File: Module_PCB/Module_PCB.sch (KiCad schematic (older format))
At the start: 102 parts, among them J1 ISP, J2 US, J3 DS, Q1 HSS2307, Q2 BSS123, U1 W25Q16JV, U2 AP1117-33, U3 TPS563200, U5 ATmega328P-AU, U7 74LVC1G34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

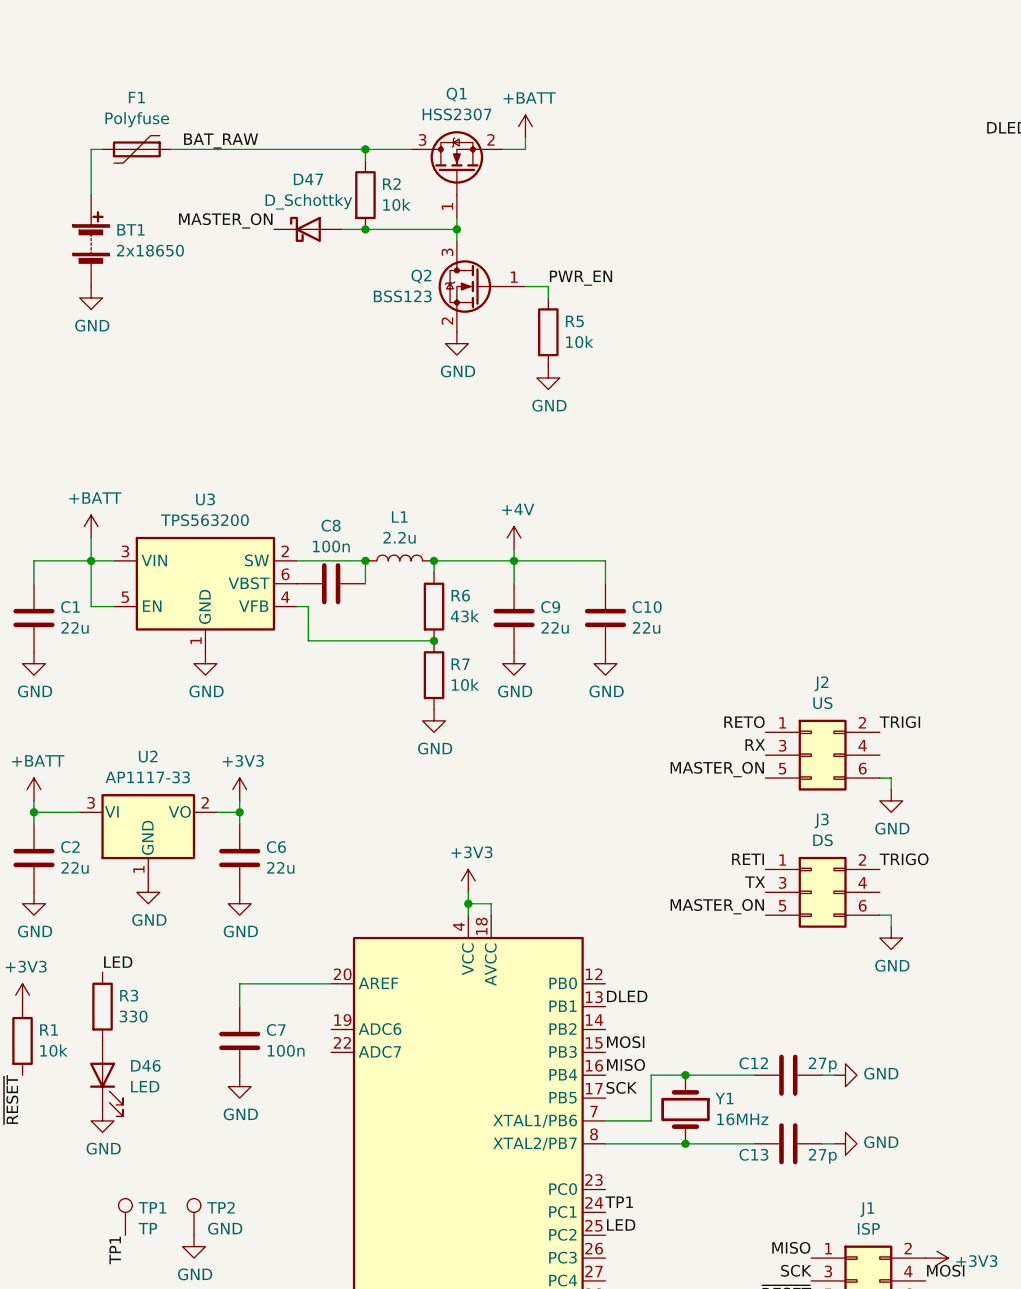
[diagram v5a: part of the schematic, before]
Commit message: Added voltage divider to measure the battery voltage
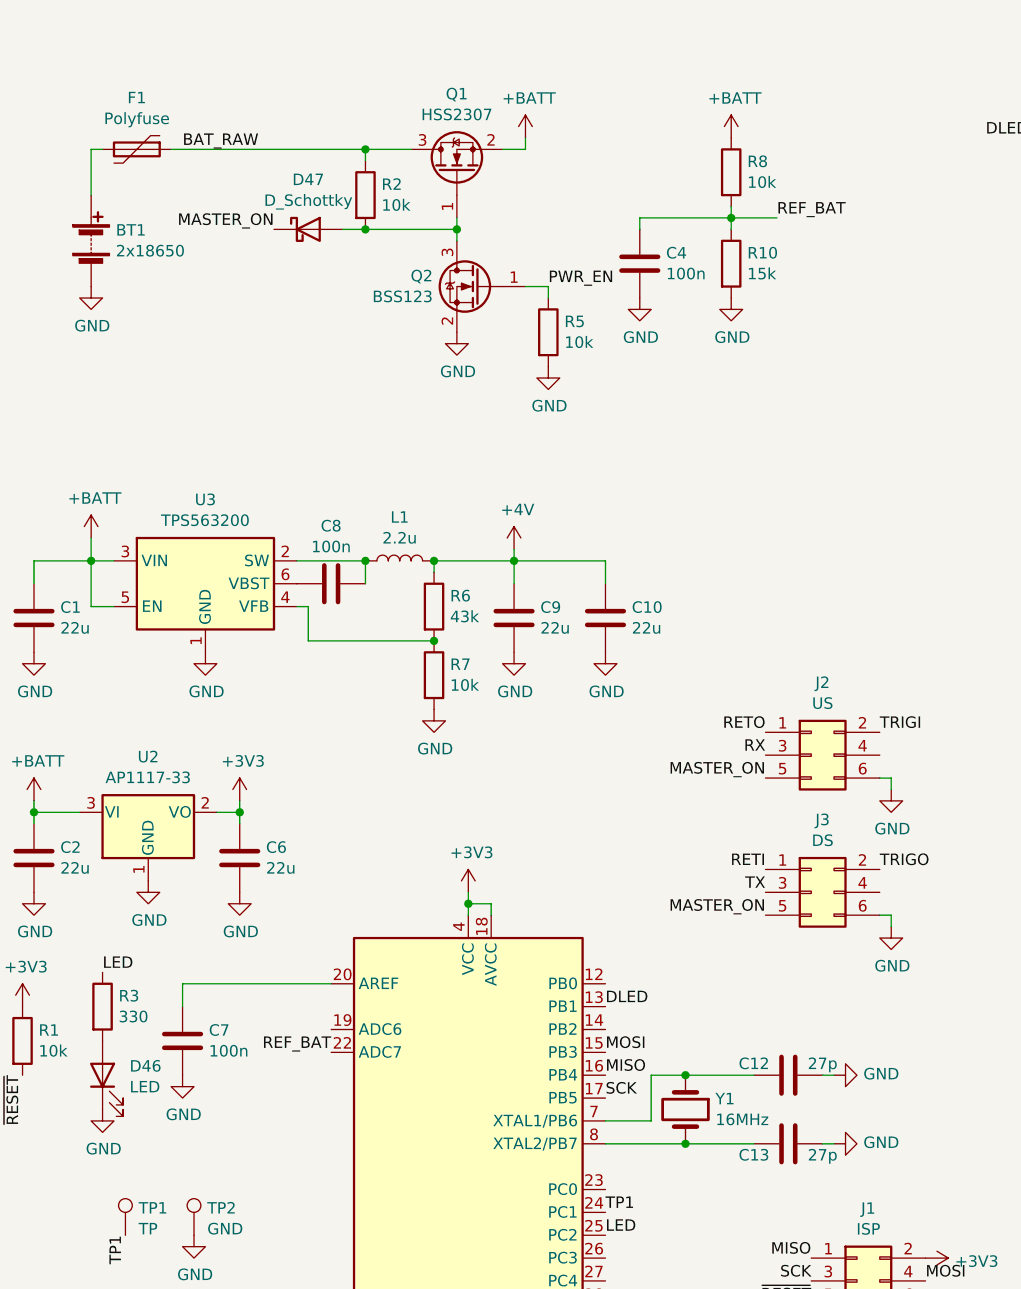
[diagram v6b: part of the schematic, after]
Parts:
- added C4: 100n, Capacitor_SMD:C_0603_1608Metric, symbol Device:C
- added R10: 15k, Resistor_SMD:R_0603_1608Metric, symbol Device:R
- added R8: 10k, Resistor_SMD:R_0603_1608Metric, symbol Device:R
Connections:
- net +BATT: now also R8.1
- net GND: now also C4.2, R10.2
- net REF_BAT: now reaches U5.22 (ADC7)
- net REF_BAT: now also C4.1, R10.1, R8.2
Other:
- moved on the sheet: C7
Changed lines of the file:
@@
 Wire Wire Line
 	2600 4350 2600 4400
-$Comp
-L Device:C C7
-U 1 1 60D68DB6
-P 1600 4950
-F 0 "C7" H 1715 4996 50  0000 L CNN
-F 1 "100n" H 1715 4905 50  0000 L CNN
-F 2 "Capacitor_SMD:C_0603_1608Metric" H 1638 4800 50  0001 C CNN
-F 3 "~" H 1600 4950 50  0001 C CNN
-F 4 "CC0603KRX7R0BB104" H 1600 4950 50  0001 C CNN "MPN"
-F 5 "YAGEO" H 1600 4950 50  0001 C CNN "Manufacturer"
-	1    1600 4950
-	1    0    0    -1
-$EndComp
-Wire Wire Line
-	2000 4700 1600 4700
-Wire Wire Line
-	1600 4700 1600 4800
-$Comp
-L power:GND #PWR018
-U 1 1 60D69990
-P 1600 5100
-F 0 "#PWR018" H 1600 4850 50  0001 C CNN
-F 1 "GND" H 1605 4927 50  0000 C CNN
-F 2 "" H 1600 5100 50  0001 C CNN
-F 3 "" H 1600 5100 50  0001 C CNN
-	1    1600 5100
-	1    0    0    -1
-$EndComp
 Text Label 3200 5200 0    50   ~ 0
 SCK
@@
 Text Label 5900 7300 0    50   ~ 0
 ~RET_EN
-Text Label 3450 7100 0    50   ~ 0
-~RET_EN
 $Comp
 L power:GND #PWR043
@@
 Wire Wire Line
 	1300 1050 2150 1050
+Text Label 2000 5000 2    50   ~ 0
+REF_BAT
+$Comp
+L power:GND #PWR018
+U 1 1 60D69990
+P 1350 5100
+F 0 "#PWR018" H 1350 4850 50  0001 C CNN
+F 1 "GND" H 1355 4927 50  0000 C CNN
+F 2 "" H 1350 5100 50  0001 C CNN
+F 3 "" H 1350 5100 50  0001 C CNN
+	1    1350 5100
+	1    0    0    -1
+$EndComp
+Wire Wire Line
+	1350 4700 1350 4800
+Wire Wire Line
+	2000 4700 1350 4700
+$Comp
+L Device:C C7
+U 1 1 60D68DB6
+P 1350 4950
+F 0 "C7" H 1465 4996 50  0000 L CNN
+F 1 "100n" H 1465 4905 50  0000 L CNN
+F 2 "Capacitor_SMD:C_0603_1608Metric" H 1388 4800 50  0001 C CNN
+F 3 "~" H 1350 4950 50  0001 C CNN
+F 4 "CC0603KRX7R0BB104" H 1350 4950 50  0001 C CNN "MPN"
+F 5 "YAGEO" H 1350 4950 50  0001 C CNN "Manufacturer"
+	1    1350 4950
+	1    0    0    -1
+$EndComp
+Text Label 3450 7100 0    50   ~ 0
+~RET_EN
+$Comp
+L power:GND #PWR0139
+U 1 1 60E13F4A
+P 3350 1700
+F 0 "#PWR0139" H 3350 1450 50  0001 C CNN
+F 1 "GND" H 3355 1527 50  0000 C CNN
+F 2 "" H 3350 1700 50  0001 C CNN
+F 3 "" H 3350 1700 50  0001 C CNN
+	1    3350 1700
+	1    0    0    -1
+$EndComp
+$Comp
+L Device:C C4
+U 1 1 60E134A1
+P 3350 1550
+F 0 "C4" H 3465 1596 50  0000 L CNN
+F 1 "100n" H 3465 1505 50  0000 L CNN
+F 2 "Capacitor_SMD:C_0603_1608Metric" H 3388 1400 50  0001 C CNN
+F 3 "~" H 3350 1550 50  0001 C CNN
+F 4 "CC0603KRX7R0BB104" H 3350 1550 50  0001 C CNN "MPN"
+F 5 "YAGEO" H 3350 1550 50  0001 C CNN "Manufacturer"
+	1    3350 1550
+	1    0    0    -1
+$EndComp
+Text Label 3950 1350 0    50   ~ 0
+REF_BAT
+Wire Wire Line
+	3750 1350 3950 1350
+Wire Wire Line
+	3750 1350 3750 1400
+Connection ~ 3750 1350
+Wire Wire Line
+	3750 1300 3750 1350
+$Comp
+L power:+BATT #PWR02
+U 1 1 60E007AC
+P 3750 1000
+F 0 "#PWR02" H 3750 850 50  0001 C CNN
+F 1 "+BATT" H 3765 1173 50  0000 C CNN
+F 2 "" H 3750 1000 50  0001 C CNN
+F 3 "" H 3750 1000 50  0001 C CNN
+	1    3750 1000
+	1    0    0    -1
+$EndComp
+$Comp
+L power:GND #PWR030
+U 1 1 60DFEFDA
+P 3750 1700
+F 0 "#PWR030" H 3750 1450 50  0001 C CNN
+F 1 "GND" H 3755 1527 50  0000 C CNN
+F 2 "" H 3750 1700 50  0001 C CNN
+F 3 "" H 3750 1700 50  0001 C CNN
+	1    3750 1700
+	1    0    0    -1
+$EndComp
+$Comp
+L Device:R R10
+U 1 1 60DFEB27
+P 3750 1550
+F 0 "R10" H 3820 1596 50  0000 L CNN
+F 1 "15k" H 3820 1505 50  0000 L CNN
+F 2 "Resistor_SMD:R_0603_1608Metric" V 3680 1550 50  0001 C CNN
+F 3 "~" H 3750 1550 50  0001 C CNN
+F 4 "YAGEO" H 3750 1550 50  0001 C CNN "Manufacturer"
+F 5 "RC0603JR-0715KL" H 3750 1550 50  0001 C CNN "MPN"
+	1    3750 1550
+	1    0    0    -1
+$EndComp
+$Comp
+L Device:R R8
+U 1 1 60DFE6E8
+P 3750 1150
+F 0 "R8" H 3820 1196 50  0000 L CNN
+F 1 "10k" H 3820 1105 50  0000 L CNN
+F 2 "Resistor_SMD:R_0603_1608Metric" V 3680 1150 50  0001 C CNN
+F 3 "~" H 3750 1150 50  0001 C CNN
+F 4 "YAGEO" H 3750 1150 50  0001 C CNN "Manufacturer"
+F 5 "RC0603JR-0710KL" H 3750 1150 50  0001 C CNN "MPN"
+	1    3750 1150
+	1    0    0    -1
+$EndComp
+Wire Wire Line
+	3750 1350 3350 1350
+Wire Wire Line
+	3350 1350 3350 1400
 $EndSCHEMATC

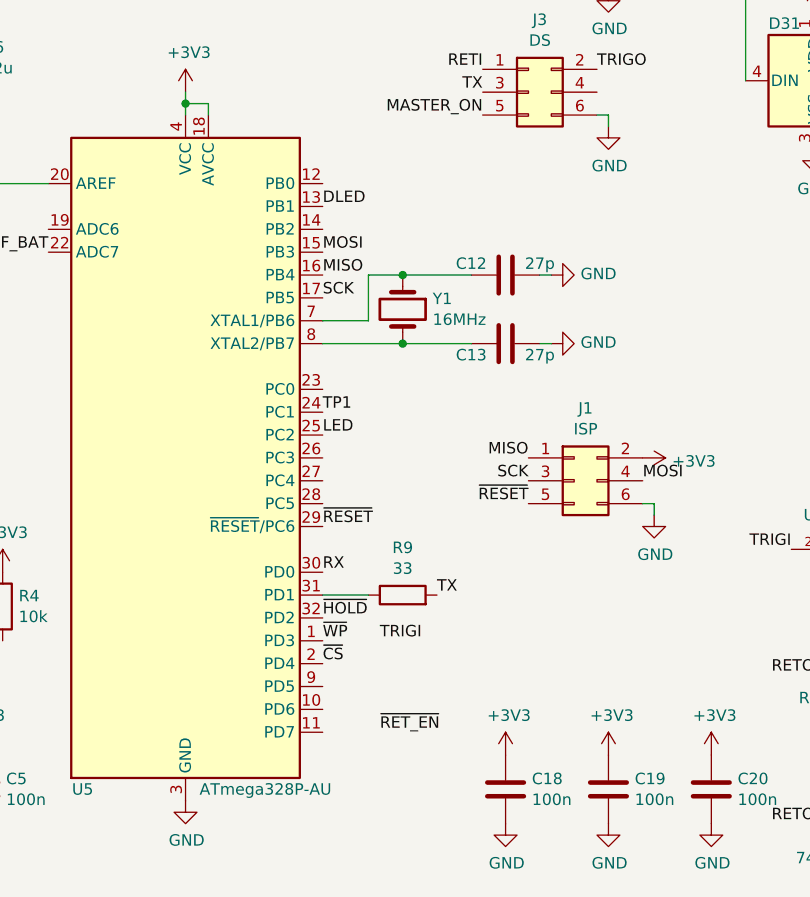
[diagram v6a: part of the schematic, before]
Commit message: Routed two signals which were forgotten
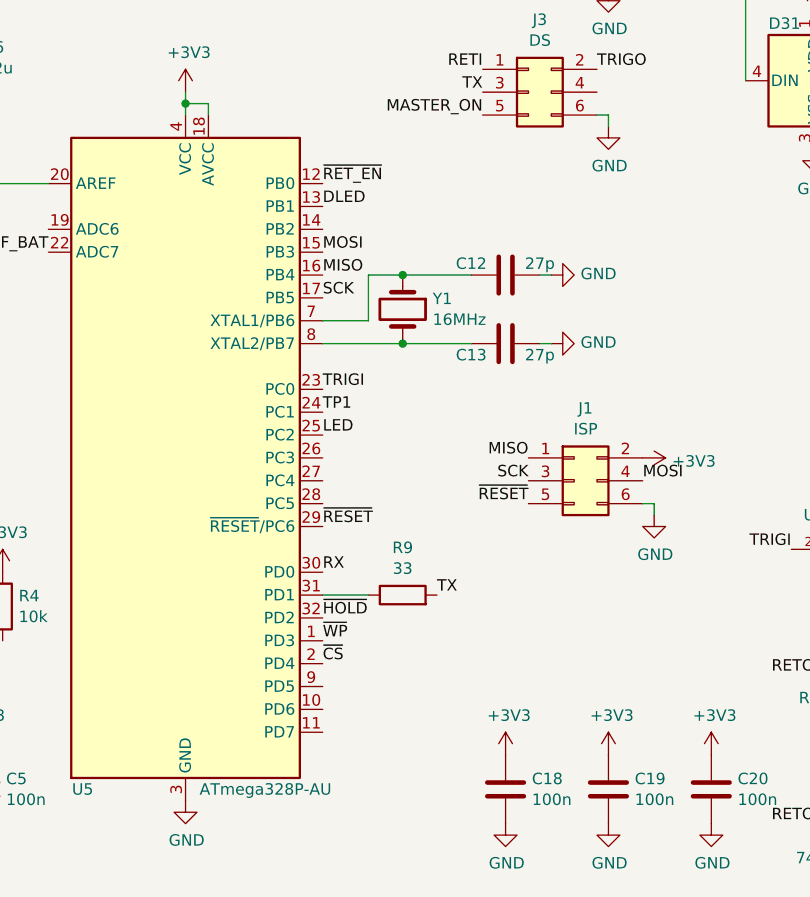
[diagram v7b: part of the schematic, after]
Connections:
- net TRIGI: now also U5.23 (PC0)
- net ~RET_EN: now also U5.12 (PB0)
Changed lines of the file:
@@
 	1    0    0    -1
 $EndComp
-Text Label 3450 6700 0    50   ~ 0
+Text Label 3200 5600 0    50   ~ 0
 TRIGI
 Text Label 5250 6300 2    50   ~ 0
@@
 	1    0    0    -1
 $EndComp
-Text Label 3450 7100 0    50   ~ 0
+Text Label 3200 4700 0    50   ~ 0
 ~RET_EN
 $Comp

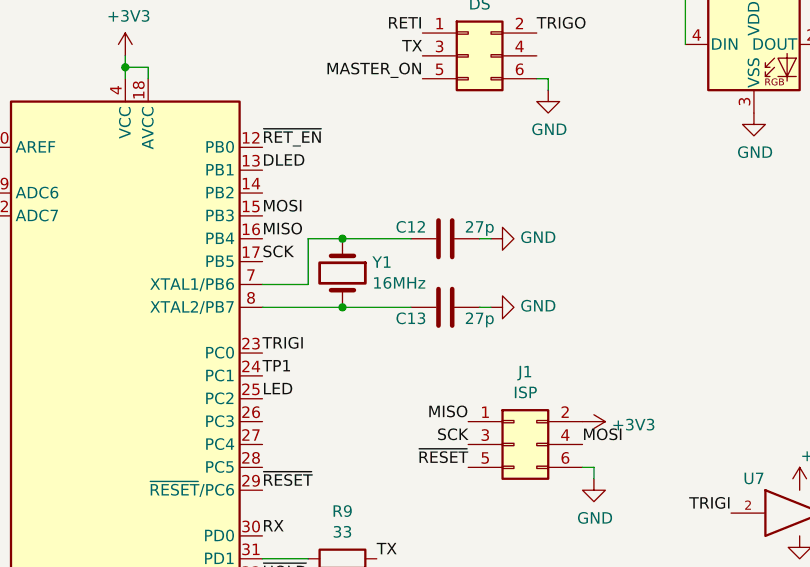
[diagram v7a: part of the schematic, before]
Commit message: Updated atmega crystal to 8 MHz
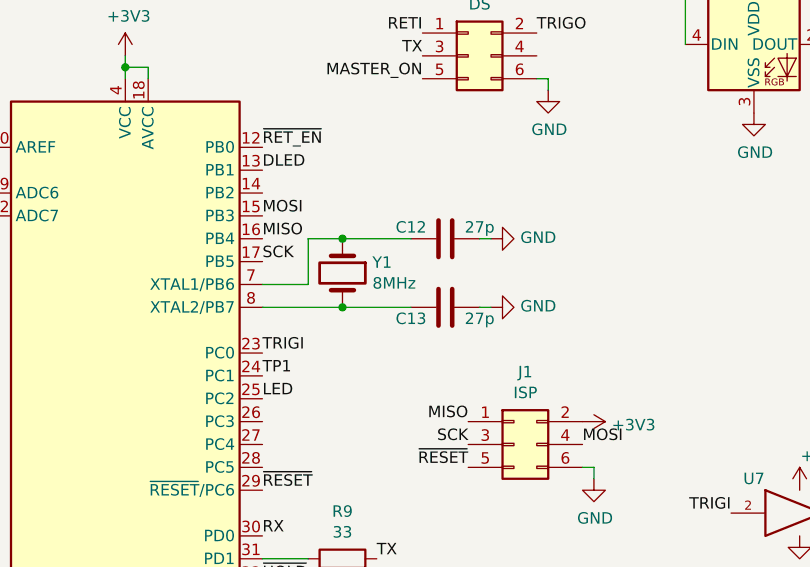
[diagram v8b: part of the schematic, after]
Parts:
- Y1: value 16MHz -> 8MHz; MPN C16000J119 -> C08000J060
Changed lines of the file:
@@
 P 3550 5250
 F 0 "Y1" V 3504 5381 50  0000 L CNN
-F 1 "16MHz" V 3595 5381 50  0000 L CNN
+F 1 "8MHz" V 3595 5381 50  0000 L CNN
 F 2 "Crystal:Crystal_SMD_HC49-SD" H 3550 5250 50  0001 C CNN
 F 3 "~" H 3550 5250 50  0001 C CNN
-F 4 "C16000J119" H 3550 5250 50  0001 C CNN "MPN"
+F 4 "C08000J060" H 3550 5250 50  0001 C CNN "MPN"
 F 5 "ECEC" H 3550 5250 50  0001 C CNN "Manufacturer"
 	1    3550 5250
